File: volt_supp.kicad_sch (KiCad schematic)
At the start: 14 parts, among them J1 input_voltage, Q1 IRML9301TRPbF, Q2 2N3906, Q3 2N3906

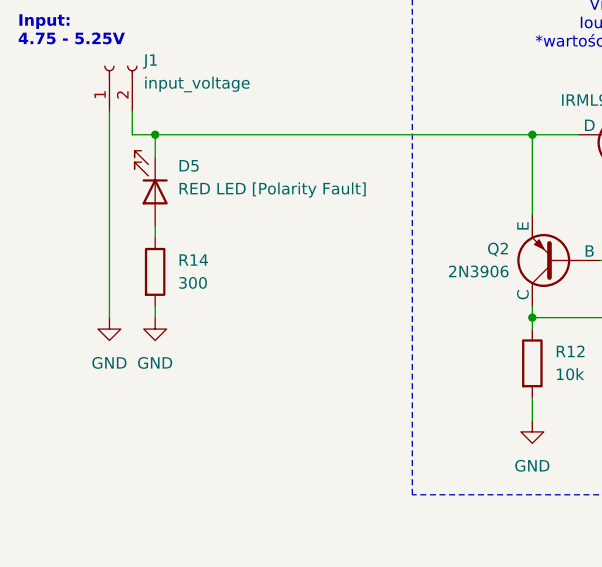
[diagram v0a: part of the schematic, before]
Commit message: Dodano brakujące footprinty do układu wejściowego i poprawiono SPI - zamieniono SCK <-> MISO (na poprawne)
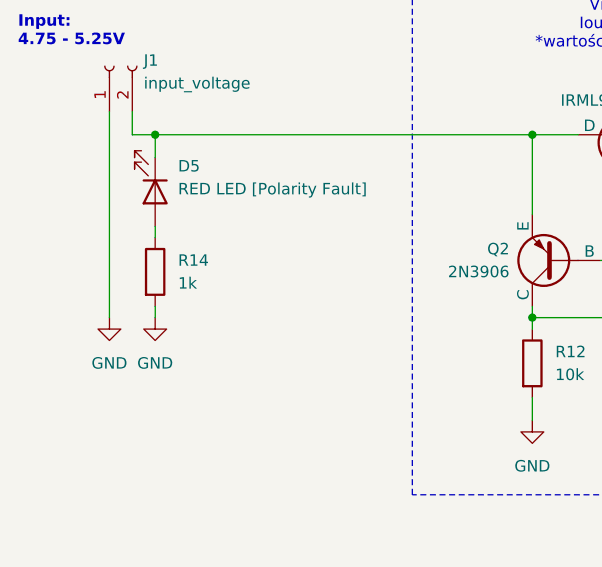
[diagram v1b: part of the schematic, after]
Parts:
- C24, C26: footprint (none) -> Capacitor_Tantalum_SMD:CP_EIA-3528-12_Kemet-T
- C25, C27: footprint (none) -> Capacitor_SMD:C_0603_1608Metric
- D5: footprint (none) -> LED_SMD:LED_0805_2012Metric
- FB1: footprint (none) -> Inductor_SMD:L_0805_2012Metric_Pad1.15x1.40mm_HandSolder
- Q1: footprint (none) -> Package_TO_SOT_SMD:SOT-23
- Q2, Q3: footprint (none) -> Package_TO_SOT_THT:TO-92L_Inline
- R12, R13: footprint (none) -> Resistor_SMD:R_0603_1608Metric
- R14: value 300 -> 1k; footprint (none) -> Resistor_SMD:R_0603_1608Metric
- TVS1: footprint (none) -> Diode_SMD:D_SMB_Handsoldering
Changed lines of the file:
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@@
 			)
 		)
-		(property "Footprint" ""
+		(property "Footprint" "Capacitor_Tantalum_SMD:CP_EIA-3528-12_Kemet-T"
 			(at 157.1752 93.98 0)
 			(effects
@@
 			)
 		)
-		(property "Footprint" ""
+		(property "Footprint" "Capacitor_SMD:C_0603_1608Metric"
 			(at 211.7852 93.98 0)
 			(effects
@@
 			)
 		)
-		(property "Footprint" ""
+		(property "Footprint" "Capacitor_SMD:C_0603_1608Metric"
 			(at 167.3352 93.98 0)
 			(effects
@@
 			)
 		)
-		(property "Footprint" ""
+		(property "Footprint" "Capacitor_Tantalum_SMD:CP_EIA-3528-12_Kemet-T"
 			(at 201.6252 93.98 0)
 			(effects
@@
 			)
 		)
-		(property "Footprint" ""
+		(property "Footprint" "Diode_SMD:D_SMB_Handsoldering"
 			(at 139.7 90.17 0)
 			(effects
@@
 			)
 		)
-		(property "Footprint" ""
+		(property "Footprint" "Package_TO_SOT_SMD:SOT-23"
 			(at 110.49 80.01 0)
 			(effects
@@
 			)
 		)
-		(property "Footprint" ""
+		(property "Footprint" "LED_SMD:LED_0805_2012Metric"
 			(at 60.96 88.9 0)
 			(effects
@@
 			)
 		)
-		(property "Value" "300"
+		(property "Value" "1k"
 			(at 63.5 99.0599 0)
 			(effects
@@
 			)
 		)
-		(property "Footprint" ""
+		(property "Footprint" "Resistor_SMD:R_0603_1608Metric"
 			(at 59.182 97.79 90)
 			(effects
@@
 			)
 		)
-		(property "Footprint" ""
+		(property "Footprint" "Resistor_SMD:R_0603_1608Metric"
 			(at 101.092 107.95 90)
 			(effects
@@
 			)
 		)
-		(property "Footprint" ""
+		(property "Footprint" "Package_TO_SOT_THT:TO-92L_Inline"
 			(at 156.21 96.52 0)
 			(effects
@@
 			)
 		)
-		(property "Footprint" ""
+		(property "Footprint" "Inductor_SMD:L_0805_2012Metric_Pad1.15x1.40mm_HandSolder"
 			(at 189.23 80.772 90)
 			(effects
@@
 			)
 		)
-		(property "Footprint" ""
+		(property "Footprint" "Package_TO_SOT_THT:TO-92L_Inline"
 			(at 69.85 96.52 0)
 			(effects
@@
 			)
 		)
-		(property "Footprint" ""
+		(property "Footprint" "Resistor_SMD:R_0603_1608Metric"
 			(at 121.412 107.95 90)
 			(effects

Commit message: dodano komentarze do projektu
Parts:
- added J12: raw_input_voltage, Connector_PinSocket_2.54mm:PinSocket_1x02_P2.54mm_Vertical, symbol Connector:Conn_01x02_Socket
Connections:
- net +5v_supply: now also J12.2 (Pin_2)
- net GND: now also J12.1 (Pin_1)
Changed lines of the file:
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@@
+	(wire
+		(pts
+			(xy 208.28 74.93) (xy 208.28 76.2)
+		)
+		(stroke
+			(width 0)
+			(type default)
+		)
+	)
 	(wire
 		(pts
@@
 		(pts
 			(xy 166.37 82.55) (xy 185.42 82.55)
+		)
+		(stroke
+			(width 0)
+			(type default)
+		)
+	)
+	(wire
+		(pts
+			(xy 210.82 74.93) (xy 210.82 82.55)
 		)
 		(stroke
@@
 		(fill
 			(type none)
-		)
-	)
-	(text_box "UWAGA\nPamiętać o rozdzieleniu na\nPCB dwóch stref GND"
-		(exclude_from_sim no)
-		(at 161.29 36.83 0)
-		(size 29.845 8.89)
-		(stroke
-			(width 0)
-			(type default)
-		)
-		(fill
-			(type none)
-		)
-		(effects
-			(font
-				(size 1.27 1.27)
-			)
-			(justify left top)
 		)
 	)
@@
 	)
 	(symbol
+		(lib_id "Connector:Conn_01x02_Socket")
+		(at 208.28 69.85 90)
+		(unit 1)
+		(exclude_from_sim no)
+		(in_bom yes)
+		(on_board yes)
+		(dnp no)
+		(fields_autoplaced yes)
+		(property "Reference" "J12"
+			(at 212.09 69.2149 90)
+			(effects
+				(font
+					(size 1.27 1.27)
+				)
+				(justify right)
+			)
+		)
+		(property "Value" "raw_input_voltage"
+			(at 212.09 71.7549 90)
+			(effects
+				(font
+					(size 1.27 1.27)
+				)
+				(justify right)
+			)
+		)
+		(property "Footprint" "Connector_PinSocket_2.54mm:PinSocket_1x02_P2.54mm_Vertical"
+			(at 208.28 69.85 0)
+			(effects
+				(font
+					(size 1.27 1.27)
+				)
+				(hide yes)
+			)
+		)
+		(property "Datasheet" "~"
+			(at 208.28 69.85 0)
+			(effects
+				(font
+					(size 1.27 1.27)
+				)
+				(hide yes)
+			)
+		)
+		(property "Description" "Generic connector, single row, 01x02, script generated"
+			(at 208.28 69.85 0)
+			(effects
+				(font
+					(size 1.27 1.27)
+				)
+				(hide yes)
+			)
+		)
+		(pin "1"
+		)
+		(pin "2"
+		)
+		(instances
+			(project "kontroler_lotu"
+				(path "/ade9c7e9-87ec-416b-ada9-3e894081f6ea/556409d6-60da-44ff-8b76-7018489c554c"
+					(reference "J12")
+					(unit 1)
+				)
+			)
+		)
+	)
+	(symbol
 		(lib_id "Device:C_Polarized")
 		(at 200.66 90.17 0)
@@
 					(unit 1)
 				)
+			)
+		)
+	)
+	(symbol
+		(lib_id "power:GND")
+		(at 208.28 76.2 0)
+		(unit 1)
+		(exclude_from_sim no)
+		(in_bom yes)
+		(on_board yes)
+		(dnp no)
+		(fields_autoplaced yes)
+		(property "Reference" "#PWR057"
+			(at 208.28 82.55 0)
+			(effects
+				(font
+					(size 1.27 1.27)
+				)
+				(hide yes)
+			)
+		)
+		(property "Value" "GND"
+			(at 208.28 81.28 0)
+			(effects
+				(font
+					(size 1.27 1.27)
+				)
+			)
+		)
+		(property "Footprint" ""
+			(at 208.28 76.2 0)
+			(effects
+				(font
+					(size 1.27 1.27)
+				)
+				(hide yes)
+			)
+		)
+		(property "Datasheet" ""
+			(at 208.28 76.2 0)
+			(effects
+				(font
+					(size 1.27 1.27)
+				)
+				(hide yes)
+			)
+		)
+		(property "Description" "Power symbol creates a global label with name \"GND\" , ground"
+			(at 208.28 76.2 0)
+			(effects
+				(font
+					(size 1.27 1.27)
+				)
+				(hide yes)
+			)
+		)
+		(pin "1"
+		)
+		(instances
+			(project "kontroler_lotu"
+				(path "/ade9c7e9-87ec-416b-ada9-3e894081f6ea/556409d6-60da-44ff-8b76-7018489c554c"
+					(reference "#PWR057")
+					(unit 1)
+				)
